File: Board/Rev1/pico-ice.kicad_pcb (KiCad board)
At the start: 4 copper layers, 22.9 x 61 mm, 99 parts, among them J1 USB_C_Receptacle_USB2.0, J2 Conn_02x20_Odd_Even, J3 Conn_02x20_Odd_Even, J4 PB_SEL, Q1 2N7002, SW1 PTS820 J25K SMTR LFS, SW2 PTS820 J25K SMTR LFS, U1 CL9293A12L5M, U2 W25Q32JVSSIQ, U3 RP2040, U4 CL9293A33L5M, U5 APS6404L-3SQN-SN, U6 ICE40UP5K-SG48ITR, U8 W25Q32JVSSIQ, Y1 12 MHz

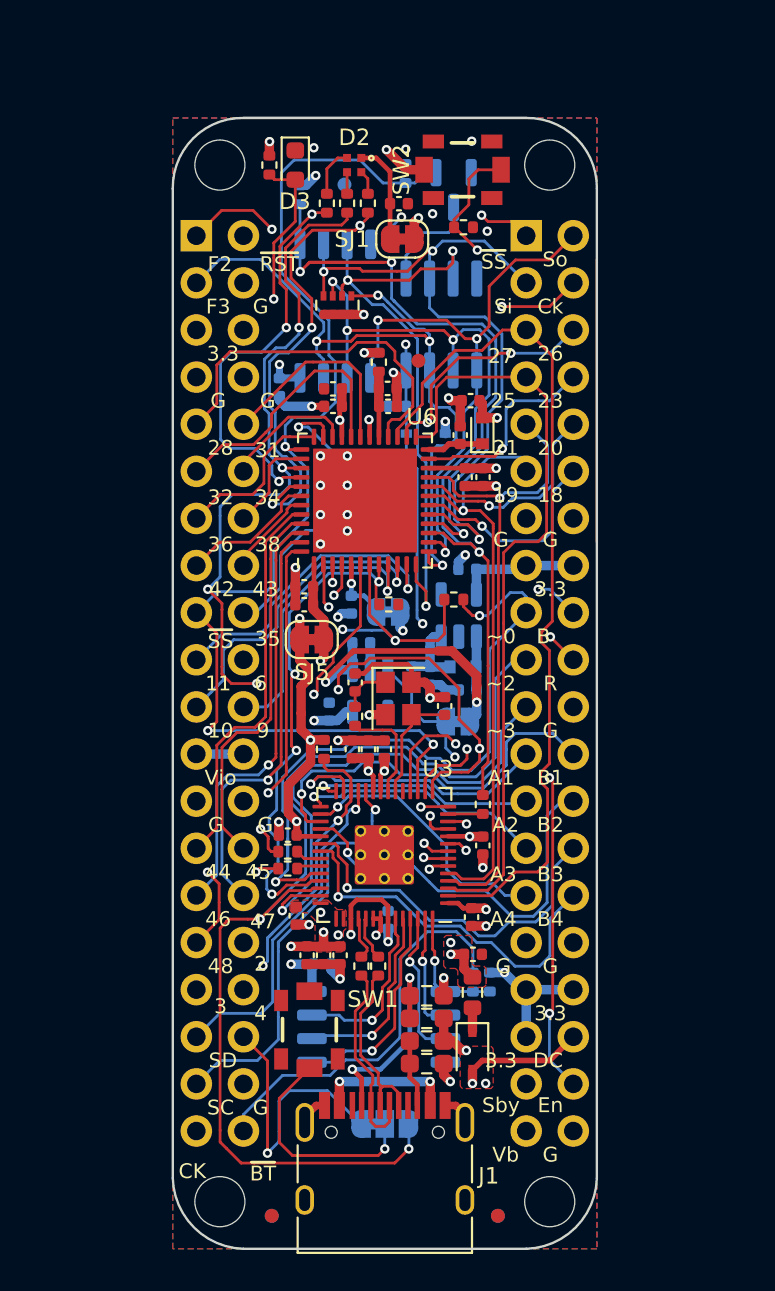
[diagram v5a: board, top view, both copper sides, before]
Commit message: Added silkscreen for PMOD identification
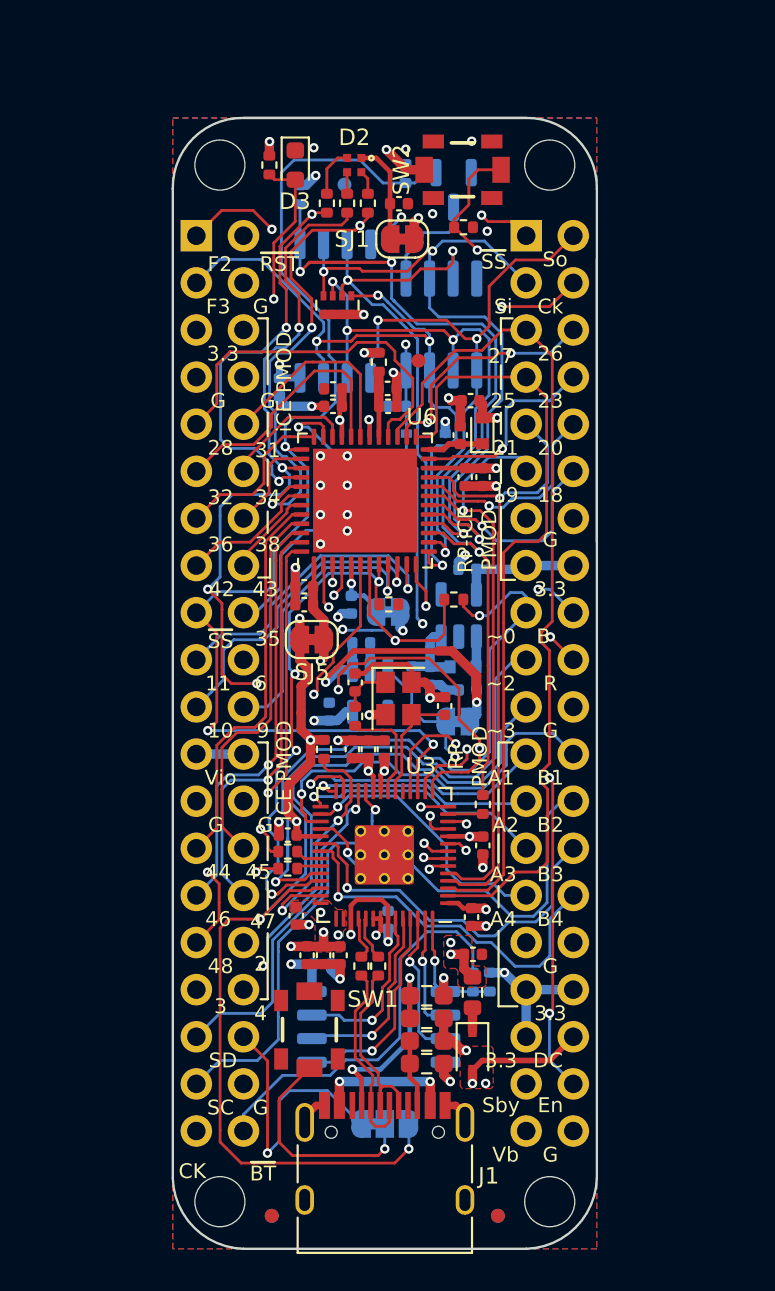
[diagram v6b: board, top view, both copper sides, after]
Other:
- board text added: "RP PMOD"
- board text added: "RP-iCE PMOD"
- board text added: "iCE PMOD"
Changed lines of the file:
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@@
     (property "Supplier" "LCSC")
     (attr smd)
-    (fp_text reference "U3" (at -2.880518 4.640129) (layer "F.SilkS")
+    (fp_text reference "U3" (at -1.966118 4.792529) (layer "F.SilkS")
       (effects (font (size 0.889 0.889) (thickness 0.127)))
     )
@@
     )
   )
+  (gr_line (start 66.202718 114.816071) (end 66.202718 116.213071) (layer "B.SilkS") (width 0.12))
+  (gr_line (start 66.202718 119.896071) (end 66.202718 121.166071) (layer "B.SilkS") (width 0.12))
+  (gr_line (start 78.648718 98.433071) (end 78.648718 98.687071) (layer "B.SilkS") (width 0.12))
+  (gr_line (start 78.394718 115.070071) (end 78.394718 116.213071) (layer "B.SilkS") (width 0.12))
   (gr_line (start 70.5358 94.107) (end 70.5358 94.1832) (layer "B.SilkS") (width 0.12))
+  (gr_line (start 78.394718 107.323071) (end 78.394718 108.593071) (layer "B.SilkS") (width 0.12))
+  (gr_line (start 65.948718 98.306071) (end 65.567718 98.306071) (layer "B.SilkS") (width 0.12))
+  (gr_line (start 78.394718 117.483071) (end 78.394718 118.880071) (layer "B.SilkS") (width 0.12))
+  (gr_line (start 78.648718 91.956071) (end 78.648718 93.353071) (layer "B.SilkS") (width 0.12))
+  (gr_line (start 65.440718 84.336071) (end 65.948718 84.336071) (layer "B.SilkS") (width 0.12))
+  (gr_line (start 65.948718 89.543071) (end 65.948718 90.940071) (layer "B.SilkS") (width 0.12))
+  (gr_line (start 78.648718 89.670071) (end 78.648718 90.813071) (layer "B.SilkS") (width 0.12))
+  (gr_line (start 78.648718 94.623071) (end 78.648718 98.433071) (layer "B.SilkS") (width 0.12))
+  (gr_line (start 78.394718 109.863071) (end 78.394718 111.260071) (layer "B.SilkS") (width 0.12))
+  (gr_line (start 66.202718 121.166071) (end 65.567718 121.166071) (layer "B.SilkS") (width 0.12))
+  (gr_line (start 79.410718 107.323071) (end 78.394718 107.323071) (layer "B.SilkS") (width 0.12))
+  (gr_line (start 78.648718 98.687071) (end 79.664718 98.687071) (layer "B.SilkS") (width 0.12))
+  (gr_line (start 65.948718 97.290071) (end 65.948718 98.306071) (layer "B.SilkS") (width 0.12))
+  (gr_line (start 78.394718 118.880071) (end 78.775718 119.261071) (layer "B.SilkS") (width 0.12))
+  (gr_line (start 65.567718 107.323071) (end 66.202718 107.323071) (layer "B.SilkS") (width 0.12))
+  (gr_line (start 78.775718 84.526571) (end 78.775718 85.669571) (layer "B.SilkS") (width 0.12))
+  (gr_line (start 78.648718 87.003071) (end 78.648718 88.146071) (layer "B.SilkS") (width 0.12))
+  (gr_line (start 79.410718 84.463071) (end 78.775718 84.463071) (layer "B.SilkS") (width 0.12))
+  (gr_line (start 65.948718 92.083071) (end 65.948718 93.353071) (layer "B.SilkS") (width 0.12))
+  (gr_line (start 78.394718 112.403071) (end 78.394718 113.800071) (layer "B.SilkS") (width 0.12))
+  (gr_line (start 65.948718 84.336071) (end 65.948718 88.146071) (layer "B.SilkS") (width 0.12))
+  (gr_line (start 66.202718 117.483071) (end 66.202718 118.626071) (layer "B.SilkS") (width 0.12))
+  (gr_line (start 78.775718 119.261071) (end 78.775718 121.674071) (layer "B.SilkS") (width 0.12))
+  (gr_line (start 66.202718 107.323071) (end 66.202718 113.673071) (layer "B.SilkS") (width 0.12))
+  (gr_line (start 78.775718 121.674071) (end 79.664718 121.674071) (layer "B.SilkS") (width 0.12))
+  (gr_line (start 65.948718 94.623071) (end 65.948718 96.020071) (layer "B.SilkS") (width 0.12))
+  (gr_line (start 78.648718 87.003071) (end 78.648718 88.273071) (layer "F.SilkS") (width 0.12))
+  (gr_line (start 65.694718 121.166071) (end 66.075718 121.166071) (layer "F.SilkS") (width 0.12))
+  (gr_line (start 66.075718 121.166071) (end 66.075718 117.610071) (layer "F.SilkS") (width 0.12))
+  (gr_line (start 65.567718 98.433071) (end 66.202718 98.433071) (layer "F.SilkS") (width 0.12))
+  (gr_line (start 66.075718 92.083071) (end 66.075718 93.480071) (layer "F.SilkS") (width 0.12))
+  (gr_line (start 79.283718 107.323071) (end 78.521718 107.323071) (layer "F.SilkS") (width 0.12))
+  (gr_line (start 78.521718 117.483071) (end 78.521718 121.547071) (layer "F.SilkS") (width 0.12))
+  (gr_line (start 66.075718 89.543071) (end 66.075718 90.813071) (layer "F.SilkS") (width 0.12))
   (gr_line (start 83.82 96.52) (end 83.82 81.28) (layer "F.SilkS") (width 0.12))
+  (gr_line (start 78.521718 121.547071) (end 79.537718 121.547071) (layer "F.SilkS") (width 0.12))
+  (gr_line (start 66.075718 111.133071) (end 66.075718 107.323071) (layer "F.SilkS") (width 0.12))
+  (gr_line (start 66.075718 84.463071) (end 66.075718 88.019071) (layer "F.SilkS") (width 0.12))
+  (gr_line (start 66.202718 98.433071) (end 66.202718 97.417071) (layer "F.SilkS") (width 0.12))
+  (gr_line (start 65.567718 84.463071) (end 66.075718 84.463071) (layer "F.SilkS") (width 0.12))
+  (gr_line (start 78.648718 84.463071) (end 78.648718 85.860071) (layer "F.SilkS") (width 0.12))
+  (gr_line (start 78.648718 98.560071) (end 79.410718 98.560071) (layer "F.SilkS") (width 0.12))
+  (gr_line (start 79.283718 84.463071) (end 78.648718 84.463071) (layer "F.SilkS") (width 0.12))
+  (gr_line (start 66.075718 116.340071) (end 66.075718 114.816071) (layer "F.SilkS") (width 0.12))
+  (gr_line (start 78.648718 94.623071) (end 78.648718 98.560071) (layer "F.SilkS") (width 0.12))
+  (gr_line (start 78.521718 107.323071) (end 78.521718 108.593071) (layer "F.SilkS") (width 0.12))
+  (gr_line (start 78.521718 115.070071) (end 78.521718 116.213071) (layer "F.SilkS") (width 0.12))
+  (gr_line (start 78.521718 109.863071) (end 78.521718 111.006071) (layer "F.SilkS") (width 0.12))
   (gr_line (start 64.77 73.66) (end 80.01 73.66) (layer "F.SilkS") (width 0.12))
+  (gr_line (start 66.075718 107.323071) (end 65.567718 107.323071) (layer "F.SilkS") (width 0.12))
+  (gr_line (start 78.648718 92.083071) (end 78.648718 93.353071) (layer "F.SilkS") (width 0.12))
+  (gr_line (start 66.075718 113.673071) (end 66.075718 112.403071) (layer "F.SilkS") (width 0.12))
+  (gr_line (start 66.075718 96.020071) (end 66.075718 94.877071) (layer "F.SilkS") (width 0.12))
+  (gr_line (start 78.521718 112.276071) (end 78.521718 113.800071) (layer "F.SilkS") (width 0.12))
+  (gr_line (start 78.648718 89.543071) (end 78.648718 90.686071) (layer "F.SilkS") (width 0.12))
   (gr_line (start 80.01 134.62) (end 64.77 134.62) (layer "Edge.Cuts") (width 0.127))
   (gr_line (start 83.82 77.47) (end 83.82 130.81) (layer "Edge.Cuts") (width 0.127))
@@
     (effects (font (size 0.8 0.8) (thickness 0.15)) (justify mirror))
   )
+  (gr_text "iCE PMOD" (at 67.599718 113.546071 90) (layer "B.SilkS")
+    (effects (font (size 1 1) (thickness 0.15)) (justify mirror))
+  )
   (gr_text "19" (at 78.775718 93.988071) (layer "B.SilkS")
     (effects (font (size 0.8 0.8) (thickness 0.15)) (justify mirror))
@@
     (effects (font (size 0.8 0.8) (thickness 0.15)) (justify mirror))
   )
+  (gr_text "RP PMOD" (at 76.743718 113.927071 90) (layer "B.SilkS")
+    (effects (font (size 1 1) (thickness 0.15)) (justify mirror))
+  )
   (gr_text "28" (at 63.535718 91.448071) (layer "B.SilkS")
     (effects (font (size 0.8 0.8) (thickness 0.15)) (justify mirror))
@@
     (effects (font (size 0.8 0.8) (thickness 0.15)) (justify mirror))
   )
-  (gr_text "G" (at 65.821718 111.768071) (layer "B.SilkS")
-    (effects (font (size 0.8 0.8) (thickness 0.15)) (justify mirror))
-  )
   (gr_text "46" (at 63.662718 116.848071) (layer "B.SilkS")
     (effects (font (size 0.8 0.8) (thickness 0.15)) (justify mirror))
@@
     (effects (font (size 0.8 0.8) (thickness 0.15)) (justify mirror))
   )
+  (gr_text "iCE PMOD" (at 67.472718 92.591071 90) (layer "B.SilkS")
+    (effects (font (size 1 1) (thickness 0.15)) (justify mirror))
+  )
   (gr_text "26" (at 81.315718 86.368071) (layer "B.SilkS")
     (effects (font (size 0.8 0.8) (thickness 0.15)) (justify mirror))
   )
+  (gr_text "RP-iCE\nPMOD" (at 76.616718 94.623071 90) (layer "B.SilkS")
+    (effects (font (size 1 1) (thickness 0.15)) (justify mirror))
+  )
   (gr_text "B" (at 81.144242 101.608071) (layer "B.SilkS")
     (effects (font (size 0.8 0.8) (thickness 0.15)) (justify mirror))
@@
     (effects (font (size 0.8 0.8) (thickness 0.15)))
   )
-  (gr_text "G" (at 78.775718 119.388071) (layer "F.SilkS")
-    (effects (font (size 0.8 0.8) (thickness 0.15)))
-  )
   (gr_text "SD" (at 63.662718 124.468071) (layer "F.SilkS")
     (effects (font (size 0.8 0.8) (thickness 0.15)))
@@
     (effects (font (size 0.8 0.8) (thickness 0.15)))
   )
+  (gr_text "RP-iCE\nPMOD" (at 77.378718 96.401071 90) (layer "F.SilkS")
+    (effects (font (size 0.8 0.8) (thickness 0.15)))
+  )
   (gr_text "B1" (at 81.315718 109.228071) (layer "F.SilkS")
     (effects (font (size 0.8 0.8) (thickness 0.15)))
@@
     (effects (font (size 0.8 0.8) (thickness 0.15)))
   )
+  (gr_text "iCE PMOD" (at 66.964718 87.892071 90) (layer "F.SilkS")
+    (effects (font (size 0.8 0.8) (thickness 0.15)))
+  )
   (gr_text "A3" (at 78.775718 114.435071) (layer "F.SilkS")
     (effects (font (size 0.8 0.8) (thickness 0.15)))
@@
     (effects (font (size 0.8 0.8) (thickness 0.15)))
   )
+  (gr_text "iCE PMOD" (at 66.964718 108.847071 90) (layer "F.SilkS")
+    (effects (font (size 0.8 0.8) (thickness 0.15)))
+  )
   (gr_text "~2" (at 78.648718 104.148071) (layer "F.SilkS")
     (effects (font (size 0.8 0.8) (thickness 0.15)))
@@
     (effects (font (size 0.8 0.8) (thickness 0.15)))
   )
-  (gr_text "44" (at 63.408718 114.308071) (layer "F.SilkS")
+  (gr_text "RP\nPMOD" (at 76.870718 108.085071 90) (layer "F.SilkS")
     (effects (font (size 0.8 0.8) (thickness 0.15)))
   )
-  (gr_text "G" (at 78.648718 96.401071) (layer "F.SilkS")
+  (gr_text "44" (at 63.408718 114.308071) (layer "F.SilkS")
     (effects (font (size 0.8 0.8) (thickness 0.15)))
   )
